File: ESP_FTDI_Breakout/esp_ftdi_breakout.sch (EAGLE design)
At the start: 3 parts

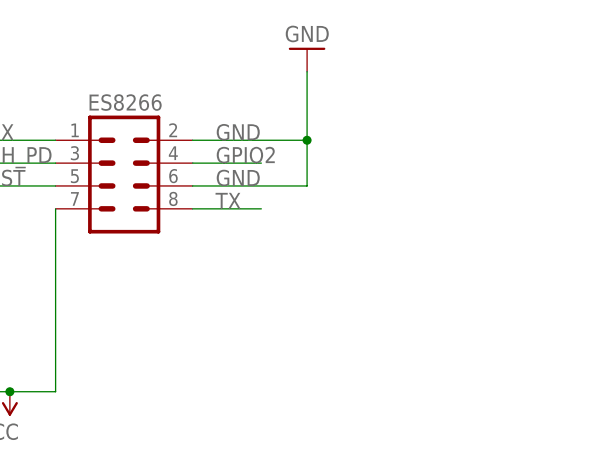
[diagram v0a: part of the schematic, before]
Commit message: Added switch to ESP_FTDI_BREAKOUT
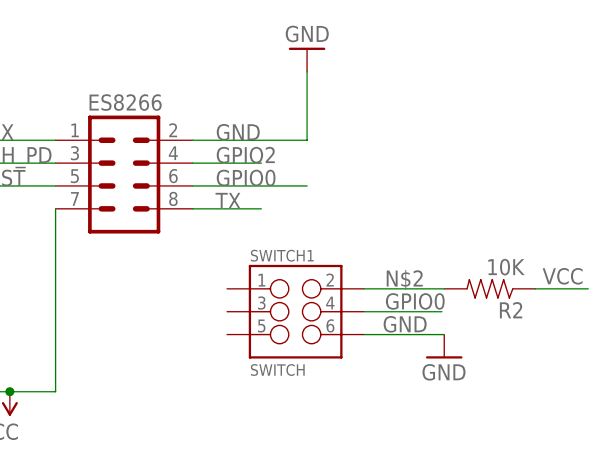
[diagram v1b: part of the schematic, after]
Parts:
- added R2: 10K, SparkFun-Resistors:1KOHM-1/4W-1%(PTH)
- added SWITCH1: SWITCH, SparkFun-Connectors:M03X2FEMALE
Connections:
- new net GPIO0: ES8266.6, SWITCH1.4
- new net N$2: R2.2, SWITCH1.2
- net GND: now also SWITCH1.6; no longer ES8266.6
- net VCC: now also R2.1
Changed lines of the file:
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@@
 <part name="GND8" library="SparkFun-Aesthetics" deviceset="GND" device=""/>
 <part name="GND1" library="SparkFun-Aesthetics" deviceset="GND" device=""/>
+<part name="SWITCH1" library="SparkFun-Connectors" deviceset="M03X2" device="FEMALE" value="SWITCH"/>
+<part name="R2" library="SparkFun-Resistors" deviceset="1KOHM-1/4W-1%(PTH)" device="" value="10K"/>
+<part name="GND2" library="SparkFun-Aesthetics" deviceset="GND" device=""/>
 </parts>
 <sheets>
@@
 <instance part="GND8" gate="1" x="30.48" y="66.04" rot="R180"/>
 <instance part="GND1" gate="1" x="81.28" y="71.12" rot="R180"/>
+<instance part="SWITCH1" gate="G$1" x="80.01" y="41.91"/>
+<instance part="R2" gate="G$1" x="101.6" y="44.45" rot="R180"/>
+<instance part="GND2" gate="1" x="96.52" y="36.83"/>
 </instances>
 <busses>
@@
 <pinref part="GND1" gate="1" pin="GND"/>
 <wire x1="81.28" y1="68.58" x2="81.28" y2="60.96" width="0.1524" layer="91"/>
-<pinref part="ES8266" gate="G$1" pin="6"/>
-<wire x1="68.58" y1="55.88" x2="81.28" y2="55.88" width="0.1524" layer="91"/>
-<label x="71.12" y="55.88" size="1.778" layer="95"/>
-<wire x1="81.28" y1="60.96" x2="81.28" y2="55.88" width="0.1524" layer="91"/>
-<junction x="81.28" y="60.96"/>
+</segment>
+<segment>
+<wire x1="87.63" y1="39.37" x2="96.52" y2="39.37" width="0.1524" layer="91"/>
+<pinref part="SWITCH1" gate="G$1" pin="6"/>
+<label x="89.662" y="39.624" size="1.778" layer="95"/>
+<pinref part="GND2" gate="1" pin="GND"/>
 </segment>
 </net>
@@
 <wire x1="53.34" y1="33.02" x2="53.34" y2="53.34" width="0.1524" layer="91"/>
 <junction x="48.26" y="33.02"/>
+</segment>
+<segment>
+<pinref part="R2" gate="G$1" pin="1"/>
+<wire x1="106.68" y1="44.45" x2="112.522" y2="44.45" width="0.1524" layer="91"/>
+<label x="107.442" y="44.958" size="1.778" layer="95"/>
 </segment>
 </net>
@@
 </segment>
 </net>
+<net name="N$2" class="0">
+<segment>
+<pinref part="SWITCH1" gate="G$1" pin="2"/>
+<wire x1="87.63" y1="44.45" x2="96.52" y2="44.45" width="0.1524" layer="91"/>
+<label x="89.916" y="44.704" size="1.778" layer="95"/>
+<pinref part="R2" gate="G$1" pin="2"/>
+</segment>
+</net>
+<net name="GPIO0" class="0">
+<segment>
+<pinref part="ES8266" gate="G$1" pin="6"/>
+<wire x1="68.58" y1="55.88" x2="81.28" y2="55.88" width="0.1524" layer="91"/>
+<label x="71.12" y="55.88" size="1.778" layer="95"/>
+</segment>
+<segment>
+<pinref part="SWITCH1" gate="G$1" pin="4"/>
+<wire x1="87.63" y1="41.91" x2="96.266" y2="41.91" width="0.1524" layer="91"/>
+<label x="89.916" y="42.164" size="1.778" layer="95"/>
+</segment>
+</net>

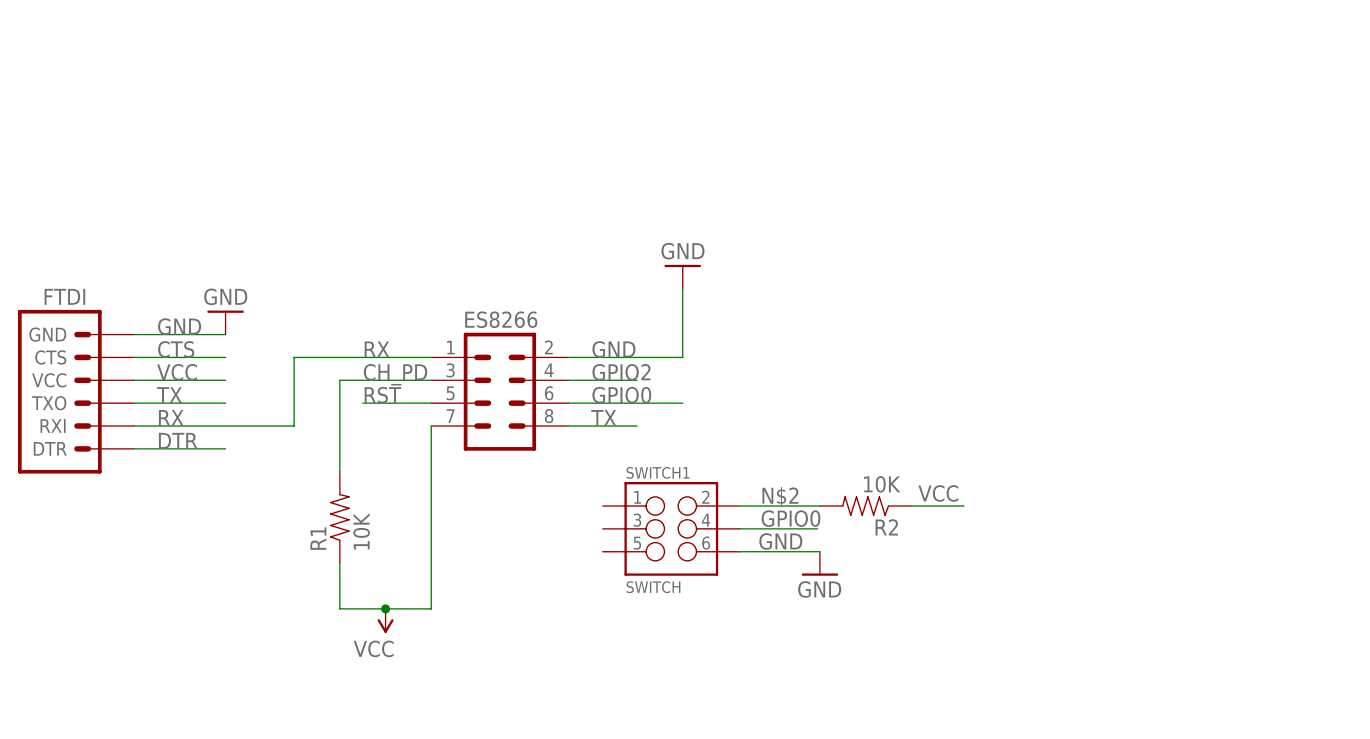
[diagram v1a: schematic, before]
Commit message: Added breakout board for connecting ESP to AVR
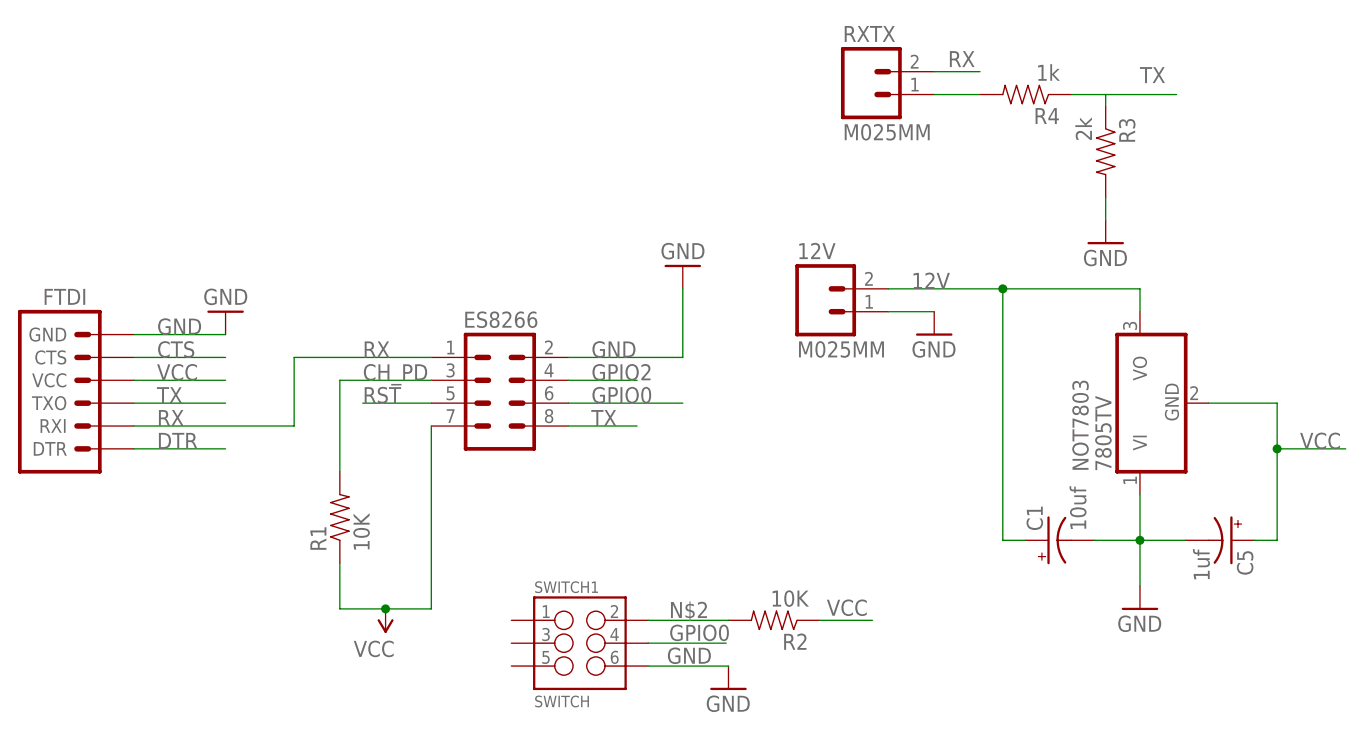
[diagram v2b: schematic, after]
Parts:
- added 12V, RXTX: M025MM, SparkFun-Connectors:M025MM
- added C1: 10uf, SparkFun-Capacitors:CAP_POLPTH2
- added C5: 1uf, SparkFun-Capacitors:CAP_POLPTH2
- added NOT7803: 7805TV, linear:7805TV
- added R3: 2k, SparkFun-Resistors:1KOHM-1/4W-1%(PTH)
- added R4: 1k, SparkFun-Resistors:1KOHM-1/4W-1%(PTH)
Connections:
- new net 12V: 12V.2, C1.+, NOT7803.VO
- new net N$1: R4.2, RXTX.1
- net GND: now also 12V.1, C1.-, C5.-, NOT7803.VI, R3.2
- net RX: now also RXTX.2
- net TX: now also R3.1, R4.1
- net VCC: now also C5.+, NOT7803.GND
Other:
- moved on the sheet: R2, SWITCH1
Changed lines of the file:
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@@
 <part name="R2" library="SparkFun-Resistors" deviceset="1KOHM-1/4W-1%(PTH)" device="" value="10K"/>
 <part name="GND2" library="SparkFun-Aesthetics" deviceset="GND" device=""/>
+<part name="RXTX" library="SparkFun-Connectors" deviceset="M02" device="5MM"/>
+<part name="12V" library="SparkFun-Connectors" deviceset="M02" device="5MM"/>
+<part name="R3" library="SparkFun-Resistors" deviceset="1KOHM-1/4W-1%(PTH)" device="" value="2k"/>
+<part name="R4" library="SparkFun-Resistors" deviceset="1KOHM-1/4W-1%(PTH)" device="" value="1k"/>
+<part name="GND3" library="SparkFun-Aesthetics" deviceset="GND" device=""/>
+<part name="C1" library="SparkFun-Capacitors" deviceset="CAP_POL" device="PTH2" value="10uf"/>
+<part name="C5" library="SparkFun-Capacitors" deviceset="CAP_POL" device="PTH2" value="1uf"/>
+<part name="NOT7803" library="linear" deviceset="78*" device="TV" technology="05">
+<attribute name="SPICEPREFIX" value="J"/>
+</part>
+<part name="GND4" library="SparkFun-Aesthetics" deviceset="GND" device=""/>
+<part name="GND5" library="SparkFun-Aesthetics" deviceset="GND" device=""/>
 </parts>
 <sheets>
@@
 <instance part="GND8" gate="1" x="30.48" y="66.04" rot="R180"/>
 <instance part="GND1" gate="1" x="81.28" y="71.12" rot="R180"/>
-<instance part="SWITCH1" gate="G$1" x="80.01" y="41.91"/>
-<instance part="R2" gate="G$1" x="101.6" y="44.45" rot="R180"/>
-<instance part="GND2" gate="1" x="96.52" y="36.83"/>
+<instance part="SWITCH1" gate="G$1" x="69.85" y="29.21"/>
+<instance part="R2" gate="G$1" x="91.44" y="31.75" rot="R180"/>
+<instance part="GND2" gate="1" x="86.36" y="24.13"/>
+<instance part="RXTX" gate="G$1" x="101.6" y="90.17"/>
+<instance part="12V" gate="G$1" x="96.52" y="66.04"/>
+<instance part="R3" gate="G$1" x="128.27" y="83.82" rot="R270"/>
+<instance part="R4" gate="G$1" x="119.38" y="90.17" rot="R180"/>
+<instance part="GND3" gate="1" x="128.27" y="73.66"/>
+<instance part="C1" gate="G$1" x="121.92" y="40.64" rot="R90"/>
+<instance part="C5" gate="G$1" x="142.24" y="40.64" rot="R270"/>
+<instance part="NOT7803" gate="A1" x="132.08" y="55.88" rot="R90"/>
+<instance part="GND4" gate="1" x="132.08" y="33.02"/>
+<instance part="GND5" gate="1" x="109.22" y="63.5"/>
 </instances>
 <busses>
@@
 </segment>
 <segment>
-<wire x1="87.63" y1="39.37" x2="96.52" y2="39.37" width="0.1524" layer="91"/>
+<wire x1="77.47" y1="26.67" x2="86.36" y2="26.67" width="0.1524" layer="91"/>
 <pinref part="SWITCH1" gate="G$1" pin="6"/>
-<label x="89.662" y="39.624" size="1.778" layer="95"/>
+<label x="79.502" y="26.924" size="1.778" layer="95"/>
 <pinref part="GND2" gate="1" pin="GND"/>
+</segment>
+<segment>
+<pinref part="12V" gate="G$1" pin="1"/>
+<wire x1="104.14" y1="66.04" x2="109.22" y2="66.04" width="0.1524" layer="91"/>
+<pinref part="GND5" gate="1" pin="GND"/>
+</segment>
+<segment>
+<pinref part="R3" gate="G$1" pin="2"/>
+<pinref part="GND3" gate="1" pin="GND"/>
+<wire x1="128.27" y1="76.2" x2="128.27" y2="78.74" width="0.1524" layer="91"/>
+</segment>
+<segment>
+<pinref part="C1" gate="G$1" pin="-"/>
+<wire x1="132.08" y1="40.64" x2="132.08" y2="35.56" width="0.1524" layer="91"/>
+<wire x1="127" y1="40.64" x2="132.08" y2="40.64" width="0.1524" layer="91"/>
+<junction x="132.08" y="40.64"/>
+<pinref part="C5" gate="G$1" pin="-"/>
+<wire x1="132.08" y1="40.64" x2="137.16" y2="40.64" width="0.1524" layer="91"/>
+<pinref part="NOT7803" gate="A1" pin="VI"/>
+<wire x1="132.08" y1="45.72" x2="132.08" y2="40.64" width="0.1524" layer="91"/>
+<pinref part="GND4" gate="1" pin="GND"/>
 </segment>
 </net>
@@
 <segment>
 <pinref part="R2" gate="G$1" pin="1"/>
-<wire x1="106.68" y1="44.45" x2="112.522" y2="44.45" width="0.1524" layer="91"/>
-<label x="107.442" y="44.958" size="1.778" layer="95"/>
+<wire x1="96.52" y1="31.75" x2="102.362" y2="31.75" width="0.1524" layer="91"/>
+<label x="97.282" y="32.258" size="1.778" layer="95"/>
+</segment>
+<segment>
+<pinref part="C5" gate="G$1" pin="+"/>
+<wire x1="147.32" y1="50.8" x2="154.94" y2="50.8" width="0.1524" layer="91"/>
+<wire x1="144.78" y1="40.64" x2="147.32" y2="40.64" width="0.1524" layer="91"/>
+<label x="149.86" y="50.8" size="1.778" layer="95"/>
+<wire x1="147.32" y1="40.64" x2="147.32" y2="50.8" width="0.1524" layer="91"/>
+<pinref part="NOT7803" gate="A1" pin="GND"/>
+<wire x1="139.7" y1="55.88" x2="147.32" y2="55.88" width="0.1524" layer="91"/>
+<wire x1="147.32" y1="55.88" x2="147.32" y2="50.8" width="0.1524" layer="91"/>
+<junction x="147.32" y="50.8"/>
 </segment>
 </net>
@@
 <wire x1="68.58" y1="53.34" x2="76.2" y2="53.34" width="0.1524" layer="91"/>
 <label x="71.12" y="53.34" size="1.778" layer="95"/>
+</segment>
+<segment>
+<pinref part="R4" gate="G$1" pin="1"/>
+<wire x1="124.46" y1="90.17" x2="128.27" y2="90.17" width="0.1524" layer="91"/>
+<wire x1="128.27" y1="90.17" x2="136.144" y2="90.17" width="0.1524" layer="91"/>
+<label x="132.08" y="91.44" size="1.778" layer="95"/>
+<pinref part="R3" gate="G$1" pin="1"/>
+<wire x1="128.27" y1="88.9" x2="128.27" y2="90.17" width="0.1524" layer="91"/>
 </segment>
 </net>
@@
 <wire x1="38.1" y1="60.96" x2="53.34" y2="60.96" width="0.1524" layer="91"/>
 </segment>
+<segment>
+<pinref part="RXTX" gate="G$1" pin="2"/>
+<wire x1="109.22" y1="92.71" x2="114.3" y2="92.71" width="0.1524" layer="91"/>
+<label x="110.744" y="93.218" size="1.778" layer="95"/>
+</segment>
 </net>
 <net name="DTR" class="0">
@@
 <segment>
 <pinref part="SWITCH1" gate="G$1" pin="2"/>
-<wire x1="87.63" y1="44.45" x2="96.52" y2="44.45" width="0.1524" layer="91"/>
-<label x="89.916" y="44.704" size="1.778" layer="95"/>
+<wire x1="77.47" y1="31.75" x2="86.36" y2="31.75" width="0.1524" layer="91"/>
+<label x="79.756" y="32.004" size="1.778" layer="95"/>
 <pinref part="R2" gate="G$1" pin="2"/>
 </segment>
@@
 <segment>
 <pinref part="SWITCH1" gate="G$1" pin="4"/>
-<wire x1="87.63" y1="41.91" x2="96.266" y2="41.91" width="0.1524" layer="91"/>
-<label x="89.916" y="42.164" size="1.778" layer="95"/>
-</segment>
-</net>
+<wire x1="77.47" y1="29.21" x2="86.106" y2="29.21" width="0.1524" layer="91"/>
+<label x="79.756" y="29.464" size="1.778" layer="95"/>
+</segment>
+</net>
+<net name="12V" class="0">
+<segment>
+<pinref part="12V" gate="G$1" pin="2"/>
+<wire x1="104.14" y1="68.58" x2="116.84" y2="68.58" width="0.1524" layer="91"/>
+<label x="106.68" y="68.58" size="1.778" layer="95"/>
+<pinref part="C1" gate="G$1" pin="+"/>
+<wire x1="119.38" y1="40.64" x2="116.84" y2="40.64" width="0.1524" layer="91"/>
+<wire x1="116.84" y1="40.64" x2="116.84" y2="68.58" width="0.1524" layer="91"/>
+<pinref part="NOT7803" gate="A1" pin="VO"/>
+<wire x1="116.84" y1="68.58" x2="132.08" y2="68.58" width="0.1524" layer="91"/>
+<wire x1="132.08" y1="68.58" x2="132.08" y2="66.04" width="0.1524" layer="91"/>
+<junction x="116.84" y="68.58"/>
+</segment>
+</net>
+<net name="N$1" class="0">
+<segment>
+<pinref part="R4" gate="G$1" pin="2"/>
+<pinref part="RXTX" gate="G$1" pin="1"/>
+<wire x1="109.22" y1="90.17" x2="114.3" y2="90.17" width="0.1524" layer="91"/>
+</segment>
+</net>
